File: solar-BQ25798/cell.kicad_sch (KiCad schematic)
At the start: 12 parts, among them Q201 DMP2035U-7, Q202 Q_PMOS_GSD, Q203 FS8205A_C908265, U201 BQ297xy

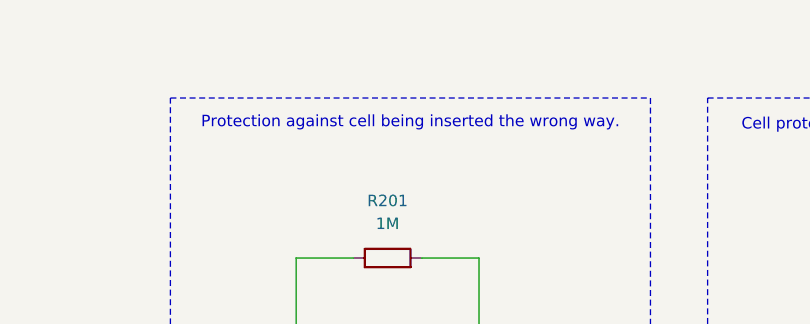
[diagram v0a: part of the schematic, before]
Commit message: Change p-mosfet and fuse LCSC part number
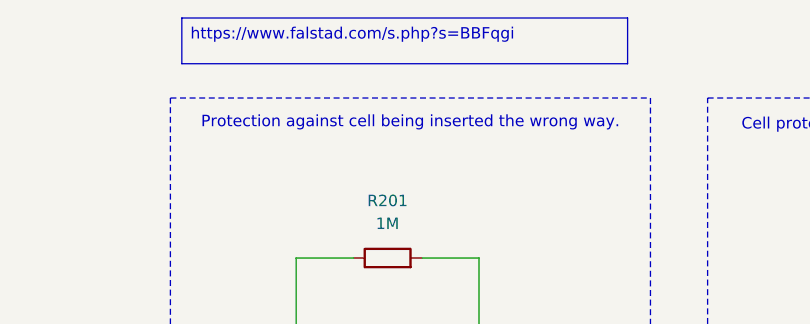
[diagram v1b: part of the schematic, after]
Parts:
- Q202: LCSC C150733 -> C3280266
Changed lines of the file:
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@@
+		)
+	)
+	(text_box "https://www.falstad.com/s.php?s=BBFqgi"
+		(exclude_from_sim no)
+		(at 81.28 27.94 0)
+		(size 49.53 5.08)
+		(margins 0.9525 0.9525 0.9525 0.9525)
+		(stroke
+			(width 0)
+			(type solid)
+		)
+		(fill
+			(type none)
+		)
+		(effects
+			(font
+				(size 1.27 1.27)
+			)
+			(justify left top)
 		)
 	)
@@
 			)
 		)
-		(property "LCSC" "C150733"
+		(property "LCSC" "C3280266"
 			(at 118.11 87.63 0)
 			(hide yes)

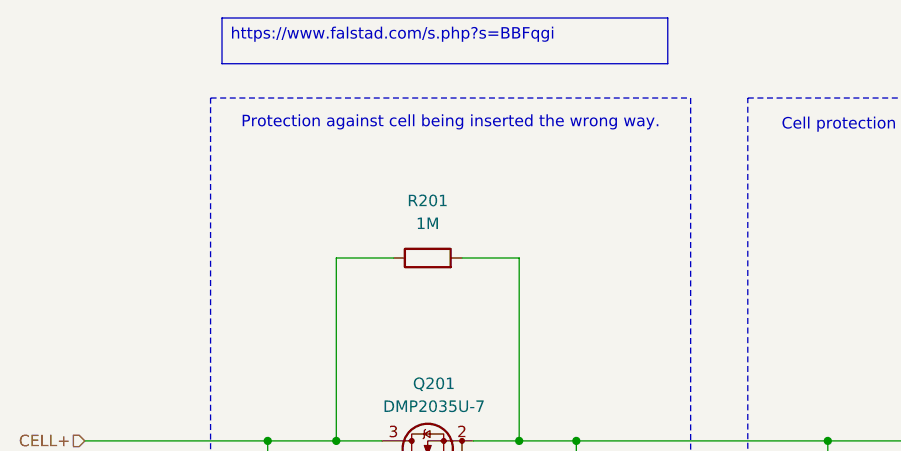
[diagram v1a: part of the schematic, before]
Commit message: Update some component parts for stock reasons
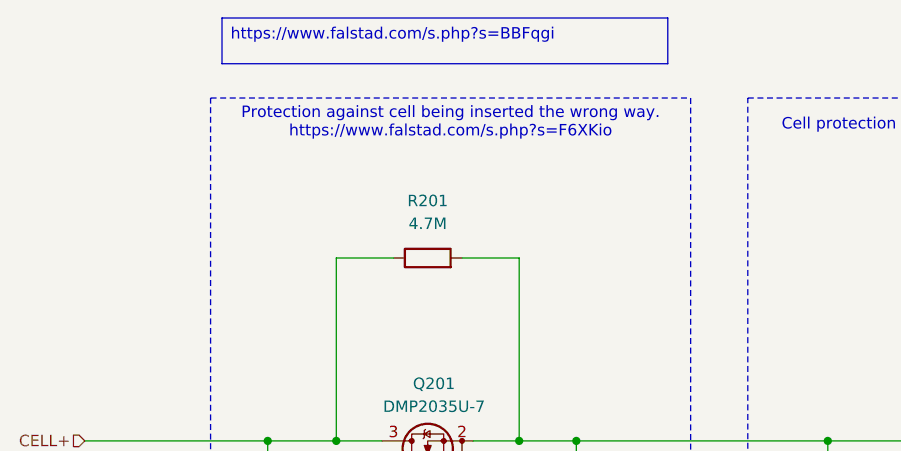
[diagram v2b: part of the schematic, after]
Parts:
- R201: value 1M -> 4.7M; LCSC Part C26083 -> C208994
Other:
- note added: "Protection against cell being inserted the wrong way. https://www.falstad.com/s.php?s=F6XKio"
- note removed: "Protection against cell being inserted the wrong way."
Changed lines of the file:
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@@
 		)
 	)
-	(text "Protection against cell being inserted the wrong way."
+	(text "Protection against cell being inserted the wrong way.\nhttps://www.falstad.com/s.php?s=F6XKio"
 		(exclude_from_sim no)
 		(at 106.68 39.624 0)
@@
 			)
 		)
-		(property "Value" "1M"
+		(property "Value" "4.7M"
 			(at 104.14 50.8 90)
 			(show_name no)
@@
 			)
 		)
-		(property "LCSC Part" "C26083"
+		(property "LCSC Part" "C208994"
 			(at 104.14 54.61 90)
 			(hide yes)

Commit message: Update LCSC part numbers
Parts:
- R201, R205, R206: LCSC Part C208994 -> C474132
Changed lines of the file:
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@@
 			)
 		)
-		(property "LCSC Part" "C208994"
+		(property "LCSC Part" "C474132"
 			(at 213.36 120.65 0)
 			(hide yes)
@@
 			)
 		)
-		(property "LCSC Part" "C208994"
+		(property "LCSC Part" "C474132"
 			(at 104.14 54.61 90)
 			(hide yes)
@@
 			)
 		)
-		(property "LCSC Part" "C208994"
+		(property "LCSC Part" "C474132"
 			(at 181.61 119.38 0)
 			(hide yes)
